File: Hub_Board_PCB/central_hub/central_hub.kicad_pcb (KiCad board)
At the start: 2 copper layers, 108 x 61.7 mm, 119 parts, among them J1 CAN_OUT, J2 Conn_01x02, J3 Screw_Terminal_01x08, J4 Screw_Terminal_01x08, J5 CSP-USC16-TR, J6 Screw_Terminal_01x04, J7 Conn_01x03, J8 Conn_01x02, J9 Screw_Terminal_01x04, Q1 BSS138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

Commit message: Testpoint location changes
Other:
- board text added: "ECE FYDP 2024 Group 26 - Ethan Gilbert - Brandon Phu - Jonathan Ko - Ben Flack"
- board text removed: "FYDP 2024 Group 26 - Ethan Gilbert - Brandon Phu - Jonathan Ko - Ben Flack"
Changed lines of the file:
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@@
   (gr_rect (start 58.503167 40.407206) (end 166.543167 102.147206)
     (stroke (width 0.2) (type default)) (fill none) (layer "Edge.Cuts"))
-  (gr_text "FYDP 2024\nGroup 26\n- Ethan Gilbert\n- Brandon Phu\n- Jonathan Ko\n- Ben Flack" (at 83.18 100.14) (layer "B.SilkS")
+  (gr_text "ECE FYDP 2024\nGroup 26\n- Ethan Gilbert\n- Brandon Phu\n- Jonathan Ko\n- Ben Flack" (at 83.18 100.14) (layer "B.SilkS")
     (effects (font (size 1.5 1.5) (thickness 0.3) bold) (justify left bottom mirror))
   )

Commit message: Central Hub USB changes
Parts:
- removed TP7, TP8: TestPoint, TestPoint:TestPoint_Pad_D1.0mm
- R1, R12, R13, R2, R4: moved to B.Cu
- moved J7 58.3 mm to (152.7, 42.0), turned to 90 degrees
- moved J9 58.3 mm to (140.5, 42.0)
- moved R4 38.2 mm to (144.7, 45.3)
- moved R13 38.0 mm to (143.2, 44.7)
- moved R12 12.8 mm to (130.5, 82.6), turned to 0 degrees
- moved C20 12.7 mm to (128.8, 60.8)
- moved C21 12.7 mm to (128.0, 59.1)
- moved C22 12.7 mm to (127.1, 57.5)
- moved J3 7.10 mm to (136.3, 42.0)
- moved R2 5.71 mm to (161.9, 90.0), turned to -90 degrees
- moved R1 5.67 mm to (161.9, 85.8), turned to 90 degrees
- moved D11 5.54 mm to (155.5, 87.7)
- moved C5 1.71 mm to (128.5, 81.1), turned to 0 degrees
- moved D10 1.10 mm to (160.0, 78.0)
- moved J5 0.53 mm to (159.7, 88.1)
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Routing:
- net +5V: track 284.7 -> 331.9 mm, vias 20 -> 24
- net ~{RESET}: track 28.1 -> 62.2 mm, vias 2 -> 1
- net BOOT: track 27.3 -> 59.2 mm, vias 2 -> 1
- net +3.3V: track 157.5 -> 182.9 mm, vias 11 -> 8
- net D8: track 35.2 -> 50.7 mm, vias 2 -> 0
- net D9: track 34.1 -> 47.8 mm, vias 2 -> 0
- net Net-(U1-NMI/INPUT_ONLY_P200): track 9.73 -> 2.91 mm, vias 0 -> 1
- net D3: track 38.0 -> 44.4 mm
- net D1: track 46.5 -> 41.9 mm, vias 2 -> 0
- net /Connectors/SHIELD2: track 30.9 -> 26.3 mm, vias 0 -> 2
- net D2: track 38.5 -> 42.5 mm
- net GND: track 55.8 -> 52.2 mm, vias 48 -> 80
- net D0: track 44.4 -> 41.5 mm, vias 2 -> 0
- net USB_D-: track 31.0 -> 29.3 mm
- net D6: track 39.1 -> 40.7 mm
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
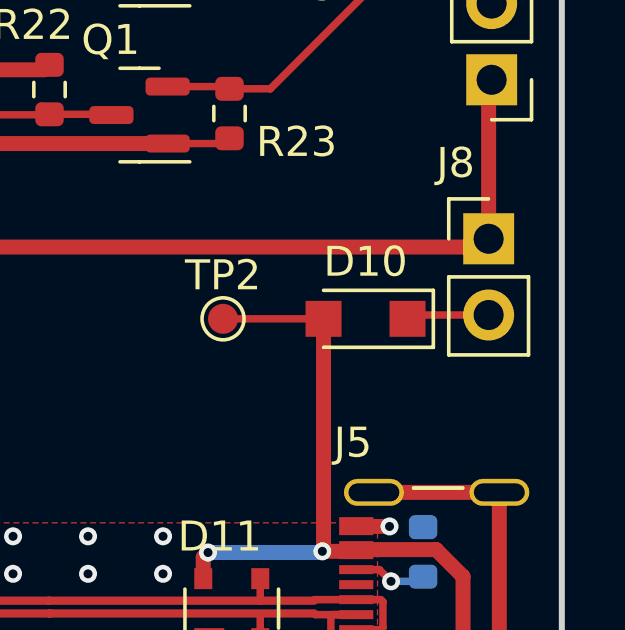
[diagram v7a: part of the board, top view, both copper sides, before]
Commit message: All usb changes on both boards
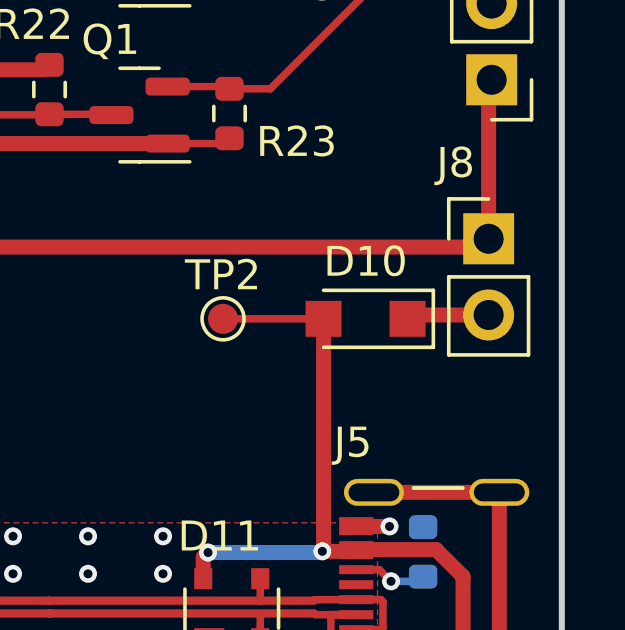
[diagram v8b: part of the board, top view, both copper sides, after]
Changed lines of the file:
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@@
     (property "ki_keywords" "cap capacitor")
     (attr smd)
-    (fp_text reference "C7" (at -0.8 1.775 180) (layer "B.SilkS")
+    (fp_text reference "C7" (at -2.1 -0.328167 180) (layer "B.SilkS")
         (effects (font (size 1 1) (thickness 0.16)) (justify mirror))
     )
@@
   (segment (start 86.353167 75.732206) (end 86.353167 73.819706) (width 0.25) (layer "F.Cu") (net 23))
   (segment (start 161.527794 77.872206) (end 161.4 78) (width 0.25) (layer "F.Cu") (net 24))
-  (segment (start 164.103167 77.872206) (end 161.527794 77.872206) (width 0.25) (layer "F.Cu") (net 24))
+  (segment (start 164.103167 77.872206) (end 161.527794 77.872206) (width 0.5) (layer "F.Cu") (net 24))
   (segment (start 155.203167 77.907206) (end 155.295961 78) (width 0.25) (layer "F.Cu") (net 25))
   (segment (start 158.6 85.71) (end 158.6 78) (width 0.5) (layer "F.Cu") (net 25))
